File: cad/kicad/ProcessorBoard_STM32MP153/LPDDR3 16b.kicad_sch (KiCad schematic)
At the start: 6 parts, among them U401 XT61M2G8D2TA-B8BEA

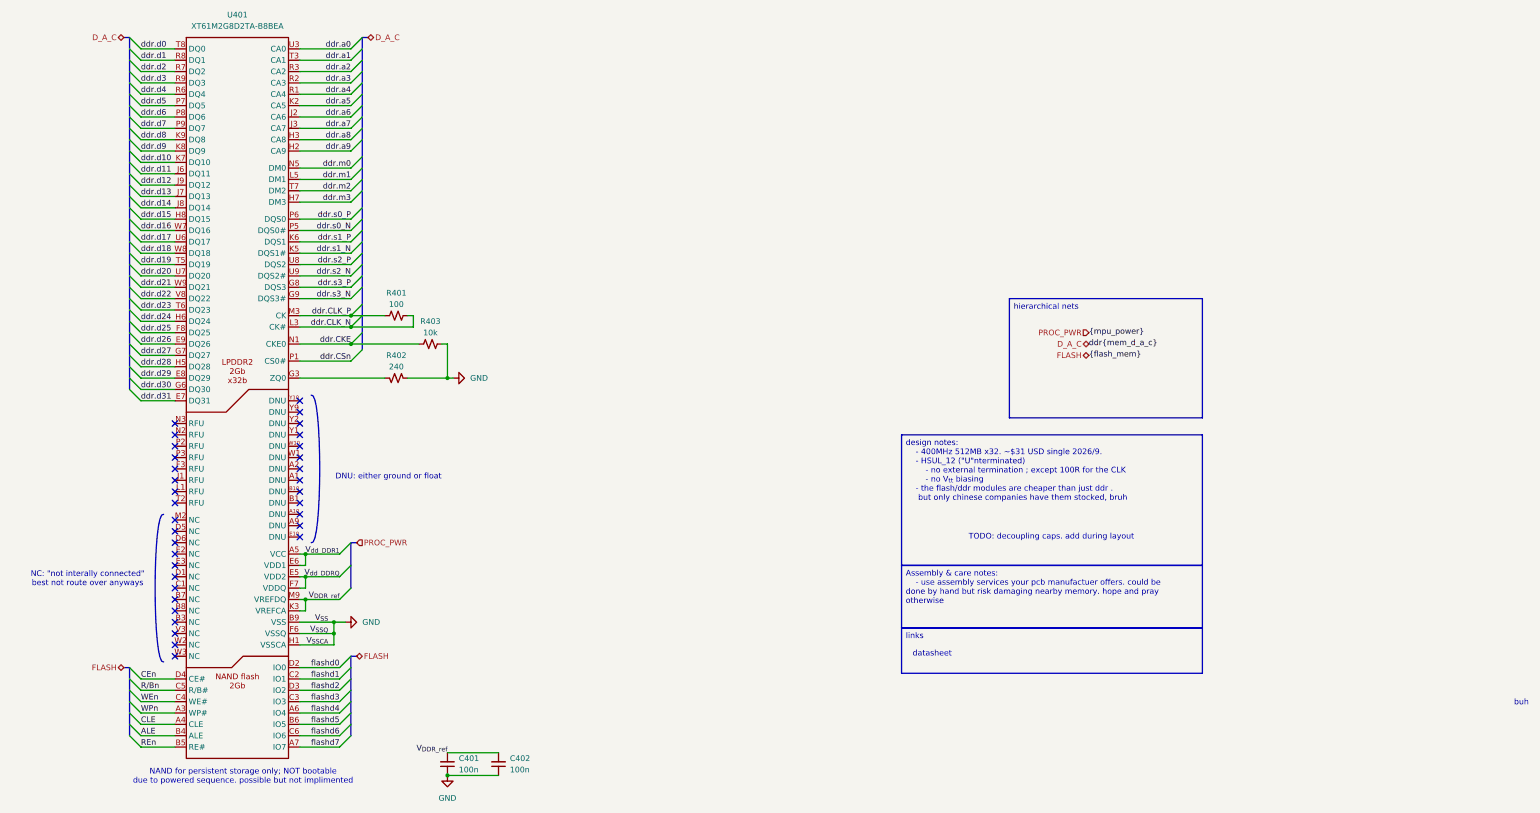
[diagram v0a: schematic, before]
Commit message: 2 layer ddr route. un tuned, missing pwr
initial ddr rout done, not lenght tuned, only impedance matched. layer 1 completely free of traces, need to put power planes on it
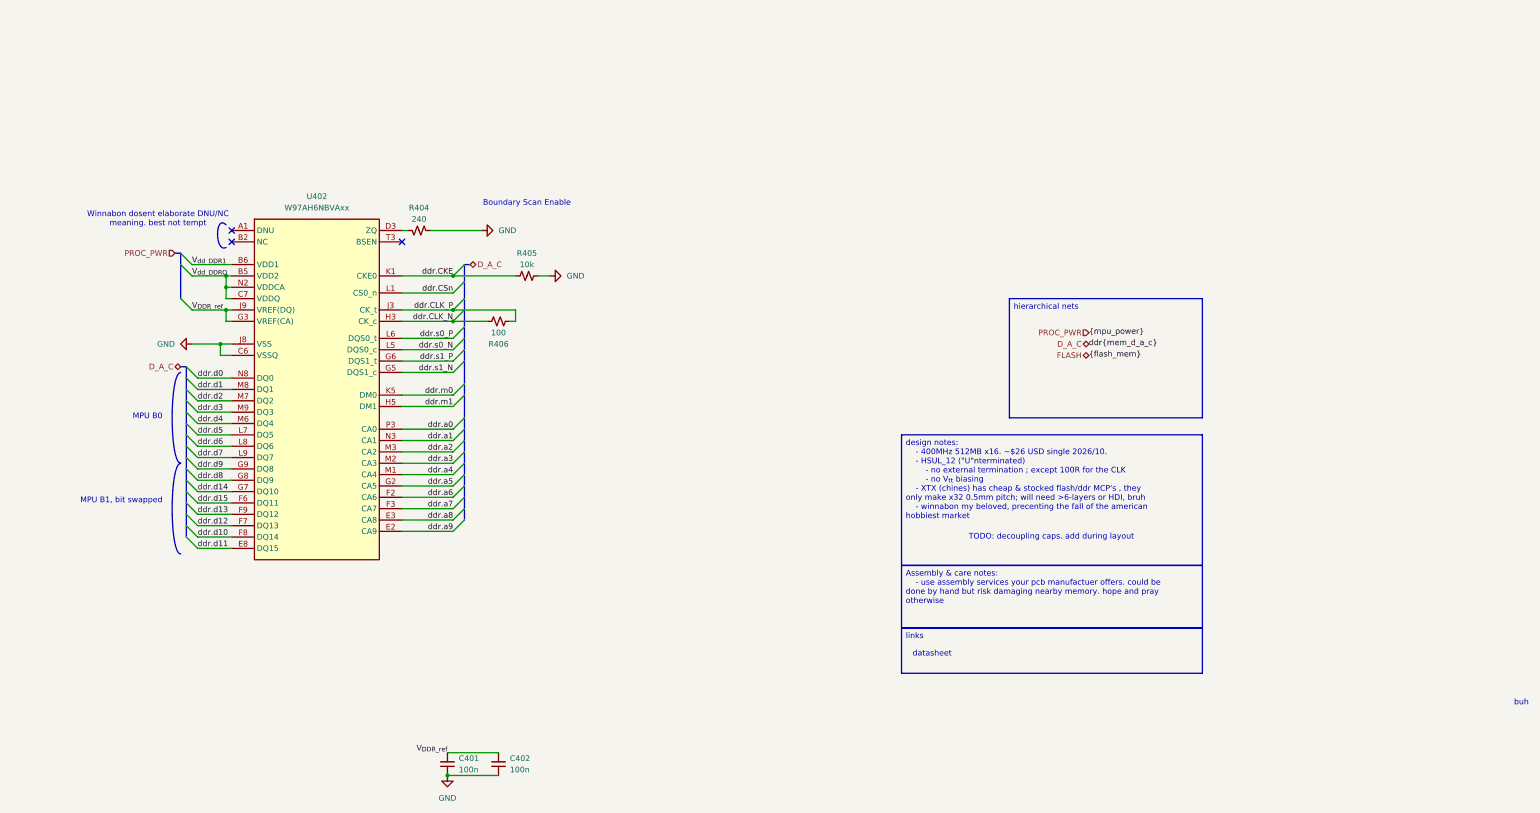
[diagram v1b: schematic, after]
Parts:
- removed R401: 100, Resistor_SMD:R_0402_1005Metric_Pad0.72x0.64mm_HandSolder, symbol Device:R_Small_US
- removed R402: 240, Capacitor_SMD:C_0402_1005Metric_Pad0.74x0.62mm_HandSolder, symbol Device:R_Small_US
- removed R403: 10k, Resistor_SMD:R_0603_1608Metric_Pad0.98x0.95mm_HandSolder, symbol Device:R_Small_US
- removed U401: XT61M2G8D2TA-B8BEA, __WM_Local:FBGA-162_L10.5-W8.0-P0.50_XT61M4G8D2TA, symbol __WM_Local:XT61M2G8D2TA-B8BEA
- added R404: 240, Capacitor_SMD:C_0402_1005Metric_Pad0.74x0.62mm_HandSolder, symbol Device:R_Small_US
- added R405: 10k, Resistor_SMD:R_0603_1608Metric_Pad0.98x0.95mm_HandSolder, symbol Device:R_Small_US
- added R406: 100, Resistor_SMD:R_0402_1005Metric_Pad0.72x0.64mm_HandSolder, symbol Device:R_Small_US
- added U402: W97AH6NBVAxx, __WM_Local:BGA134C65P10X17_1000X1150X110, symbol __WM_Local:W97AH6NBVAxx
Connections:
- net GND: now also R404.2, R405.2, U402.C2 (VSS), U402.C5 (VSS), U402.C6 (VSSQ), U402.C9 (VSSQ), U402.D1 (VSS), U402.D10 (VSSQ), U402.E1 (VSS), U402.E10 (VSSQ), U402.F5 (VSSQ), U402.G10 (VSSQ), U402.H2 (VSS), U402.J1 (VSS), U402.J5 (VSSQ), U402.J8 (VSS), U402.L10 (VSSQ), U402.M5 (VSSQ), U402.N1 (VSS), U402.N10 (VSSQ), U402.P1 (VSS), U402.P10 (VSSQ), U402.R2 (VSS), U402.R5 (VSS), U402.R6 (VSSQ), U402.R9 (VSSQ)
- net V_{DDR_ref}: now also U402.G3 (VREF(CA)), U402.J9 (VREF(DQ))
- net V_{dd_DDR1}: now also U402.B6 (VDD1), U402.C1 (VDD1), U402.R1 (VDD1), U402.T6 (VDD1)
- net V_{dd_DDRQ}: now also U402.B5 (VDD2), U402.C10 (VDDQ), U402.C7 (VDDQ), U402.D2 (VDD2), U402.D5 (VDDQ), U402.E9 (VDDQ), U402.F1 (VDDCA), U402.F10 (VDDQ), U402.G1 (VDD2), U402.H1 (VDDCA), U402.H6 (VDDQ), U402.J6 (VDDQ), U402.J7 (VDD2), U402.K6 (VDDQ), U402.M10 (VDDQ), U402.N2 (VDDCA), U402.N9 (VDDQ), U402.P2 (VDD2), U402.P5 (VDDQ), U402.R10 (VDDQ), U402.R7 (VDDQ), U402.T5 (VDD2)
- net ddr.CKE: now also R405.1, U402.K1 (CKE0)
- net ddr.CLK_N: now also R406.2, U402.H3 (CK_c)
- net ddr.CLK_P: now also R406.1, U402.J3 (CK_t)
- net ddr.CSn: now also U402.L1 (CS0_n)
- net ddr.a0: now also U402.P3 (CA0)
- net ddr.a1: now also U402.N3 (CA1)
- net ddr.a2: now also U402.M3 (CA2)
- net ddr.a3: now also U402.M2 (CA3)
- net ddr.a4: now also U402.M1 (CA4)
- net ddr.a5: now also U402.G2 (CA5)
- net ddr.a6: now also U402.F2 (CA6)
- net ddr.a7: now also U402.F3 (CA7)
- net ddr.a8: now also U402.E3 (CA8)
- net ddr.a9: now also U402.E2 (CA9)
- net ddr.d0: now also U402.N8 (DQ0)
- net ddr.d1: now also U402.M8 (DQ1)
- net ddr.d10: now also U402.F8 (DQ14)
- net ddr.d11: now also U402.E8 (DQ15)
- net ddr.d12: now also U402.F7 (DQ13)
- net ddr.d13: now also U402.F9 (DQ12)
- net ddr.d14: now also U402.G7 (DQ10)
- net ddr.d15: now also U402.F6 (DQ11)
- net ddr.d2: now also U402.M7 (DQ2)
- net ddr.d3: now also U402.M9 (DQ3)
- net ddr.d4: now also U402.M6 (DQ4)
- net ddr.d5: now also U402.L7 (DQ5)
- net ddr.d6: now also U402.L8 (DQ6)
- net ddr.d7: now also U402.L9 (DQ7)
- net ddr.d8: now also U402.G8 (DQ9)
- net ddr.d9: now also U402.G9 (DQ8)
- net ddr.m0: now also U402.K5 (DM0)
- net ddr.m1: now also U402.H5 (DM1)
- net ddr.s0_N: now also U402.L5 (DQS0_c)
- net ddr.s0_P: now also U402.L6 (DQS0_t)
- net ddr.s1_N: now also U402.G5 (DQS1_c)
- net ddr.s1_P: now also U402.G6 (DQS1_t)
- new net: U402.A1 (DNU), U402.A10 (DNU), U402.A2 (DNU), U402.A9 (DNU), U402.B1 (DNU), U402.B10 (DNU), U402.T1 (DNU), U402.T10 (DNU), U402.U1 (DNU), U402.U10 (DNU), U402.U2 (DNU), U402.U9 (DNU)
- new net: U402.B2 (NC), U402.B3 (NC), U402.B7 (NC), U402.B8 (NC), U402.B9 (NC), U402.C3 (NC), U402.C8 (NC), U402.D6 (NC), U402.D7 (NC), U402.D8 (NC), U402.D9 (NC), U402.E5 (NC), U402.E6 (NC), U402.E7 (NC), U402.J2 (NC), U402.K2 (NC), U402.K3 (NC), U402.L2 (NC), U402.L3 (NC), U402.N5 (NC), U402.N6 (NC), U402.N7 (NC), U402.P6 (NC), U402.P7 (NC), U402.P8 (NC), U402.P9 (NC), U402.R3 (NC), U402.R8 (NC), U402.T2 (NC), U402.T7 (NC), U402.T8 (NC), U402.T9 (NC)
- new net: R404.1, U402.D3 (ZQ)
- no-connect marks 34 -> 3
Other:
- note added: "Boundary Scan Enable"
- note added: "MPU B0"
- note added: "MPU B1, bit swapped"
- note added: "Winnabon dosent elaborate DNU/NC meaning. best not tempt"
- note removed: "DNU: either ground or float"
- note removed: "NAND for persistent storage only; NOT bootable due to powered sequence. possible but not implimented"
- note removed: "NC: "not interally connected" best not route over anyways"

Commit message: good enuff routing
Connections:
- net ddr.d11: now also U402.F7 (DQ13); no longer U402.E8 (DQ15)
- net ddr.d12: now also U402.E8 (DQ15); no longer U402.F7 (DQ13)
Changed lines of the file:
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@@
 	)
 	(label "ddr.d11"
-		(at 58.42 137.16 0)
+		(at 58.42 132.08 0)
 		(effects
 			(font
@@
 	)
 	(label "ddr.d12"
-		(at 58.42 132.08 0)
+		(at 58.42 137.16 0)
 		(effects
 			(font

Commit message: boo womp 10000
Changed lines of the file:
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@@
 	(text "Boundary Scan Enable\n"
 		(exclude_from_sim no)
-		(at 132.08 59.944 0)
+		(at 105.918 68.834 0)
 		(effects
 			(font
 				(size 1.27 1.27)
 			)
+			(justify left)
 		)
 	)

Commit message: i forgor track spacing :(
need to redo ddr
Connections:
- net ddr.d10: now also U402.G7 (DQ10); no longer U402.F8 (DQ14)
- net ddr.d12: now also U402.F9 (DQ12); no longer U402.E8 (DQ15)
- net ddr.d13: now also U402.E8 (DQ15); no longer U402.F9 (DQ12)
- net ddr.d14: now also U402.F8 (DQ14); no longer U402.G7 (DQ10)
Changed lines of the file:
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@@
 	)
 	(label "ddr.d13"
-		(at 58.42 129.54 0)
+		(at 58.42 137.16 0)
 		(effects
 			(font
@@
 	)
 	(label "ddr.d12"
-		(at 58.42 137.16 0)
+		(at 58.42 129.54 0)
 		(effects
 			(font
@@
 	)
 	(label "ddr.d14"
-		(at 58.42 124.46 0)
+		(at 58.42 134.62 0)
 		(effects
 			(font
@@
 	)
 	(label "ddr.d10"
-		(at 58.42 134.62 0)
+		(at 58.42 124.46 0)
 		(effects
 			(font

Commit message: ddr shuffle maxxing round 2
mostly hitting the 3w and 4w spacing. one must hope. #hope
ive disabled DRC for optimal routing experience . ching chong over clank ckong any day(until i get the good stuff) has nothing on the sweat shop.
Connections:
- net ddr.d10: now also U402.E8 (DQ15); no longer U402.G7 (DQ10)
- net ddr.d11: now also U402.F8 (DQ14); no longer U402.F7 (DQ13)
- net ddr.d12: now also U402.F6 (DQ11); no longer U402.F9 (DQ12)
- net ddr.d13: now also U402.F7 (DQ13); no longer U402.E8 (DQ15)
- net ddr.d14: now also U402.F9 (DQ12); no longer U402.F8 (DQ14)
- net ddr.d15: now also U402.G8 (DQ9); no longer U402.F6 (DQ11)
- net ddr.d8: now also U402.G7 (DQ10); no longer U402.G8 (DQ9)
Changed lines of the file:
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@@
 	)
 	(label "ddr.d8"
-		(at 58.42 121.92 0)
+		(at 58.42 124.46 0)
 		(effects
 			(font
@@
 	)
 	(label "ddr.d13"
-		(at 58.42 137.16 0)
+		(at 58.42 132.08 0)
 		(effects
 			(font
@@
 	)
 	(label "ddr.d11"
-		(at 58.42 132.08 0)
+		(at 58.42 134.62 0)
 		(effects
 			(font
@@
 	)
 	(label "ddr.d12"
-		(at 58.42 129.54 0)
+		(at 58.42 127 0)
 		(effects
 			(font
@@
 	)
 	(label "ddr.d14"
-		(at 58.42 134.62 0)
+		(at 58.42 129.54 0)
 		(effects
 			(font
@@
 	)
 	(label "ddr.d15"
-		(at 58.42 127 0)
+		(at 58.42 121.92 0)
 		(effects
 			(font
@@
 	)
 	(label "ddr.d10"
-		(at 58.42 124.46 0)
-		(effects
-			(font
+		(at 58.42 137.16 0)
+		(effects
+			(font

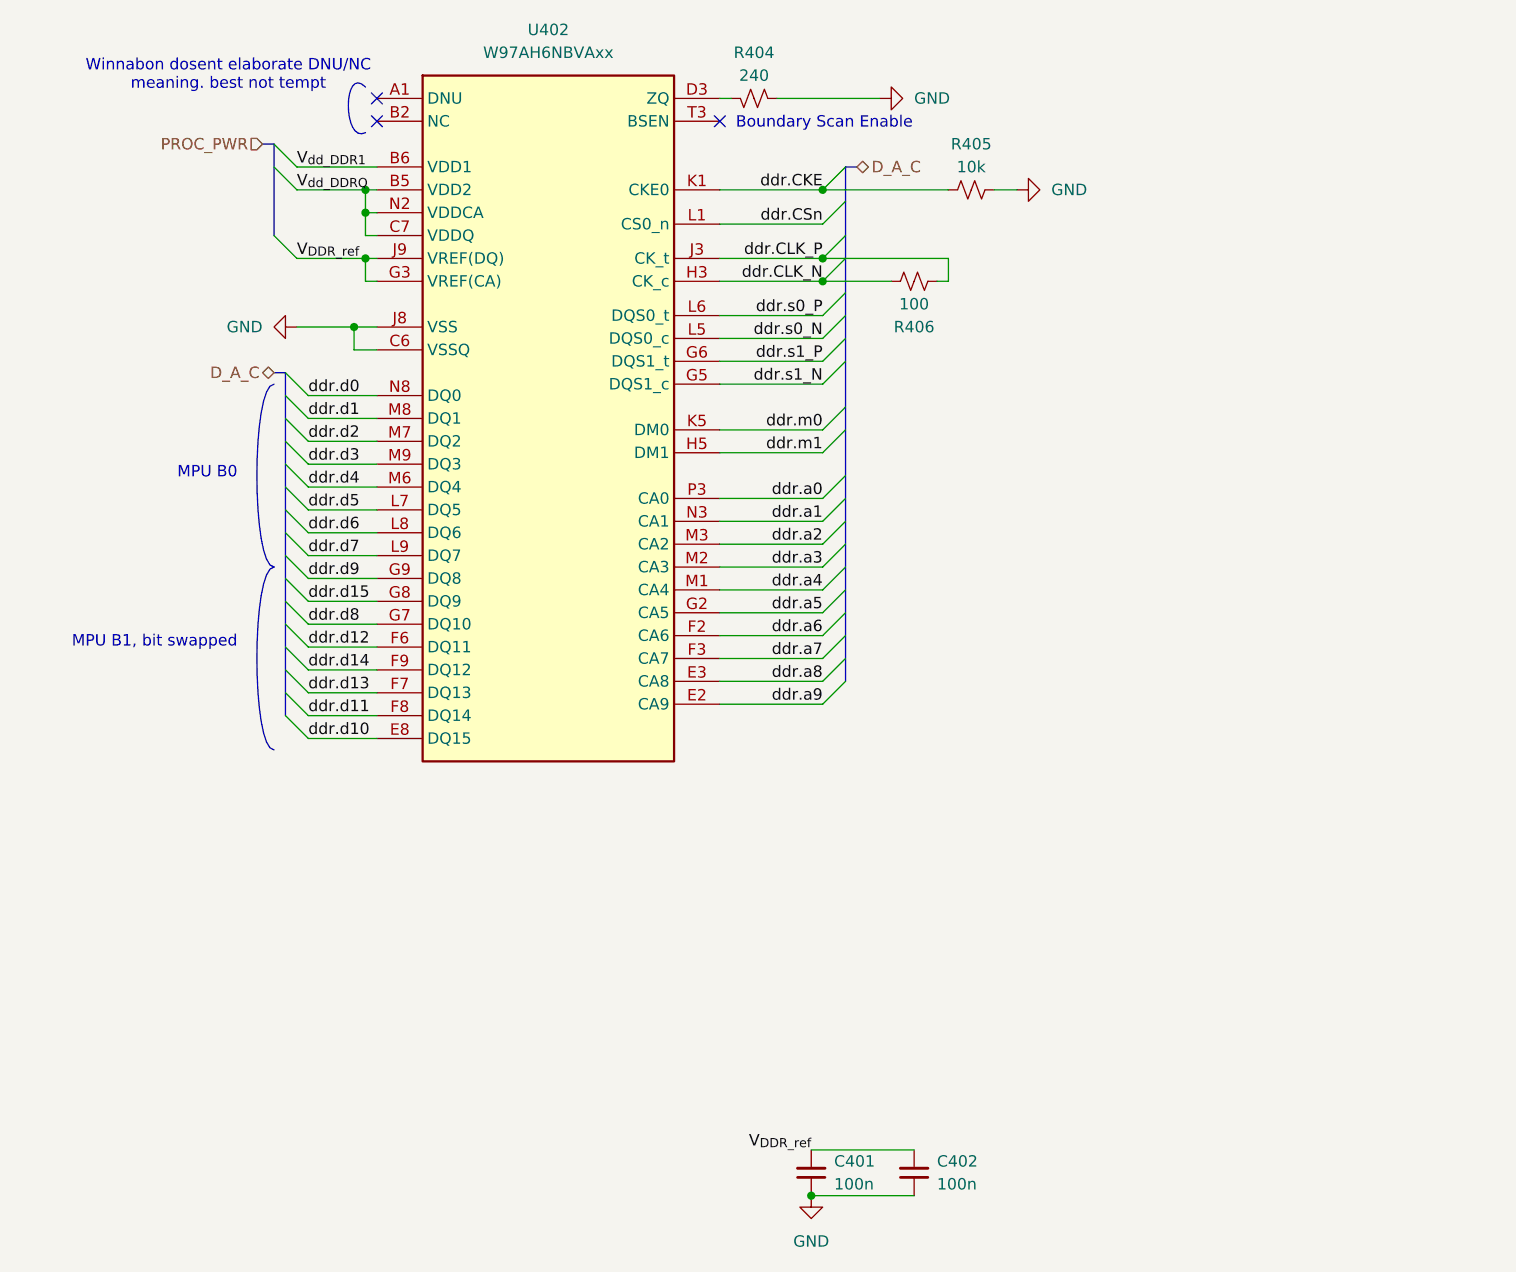
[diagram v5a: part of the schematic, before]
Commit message: shuffled core back to left side of board, fits better
row row the power planes under mpu
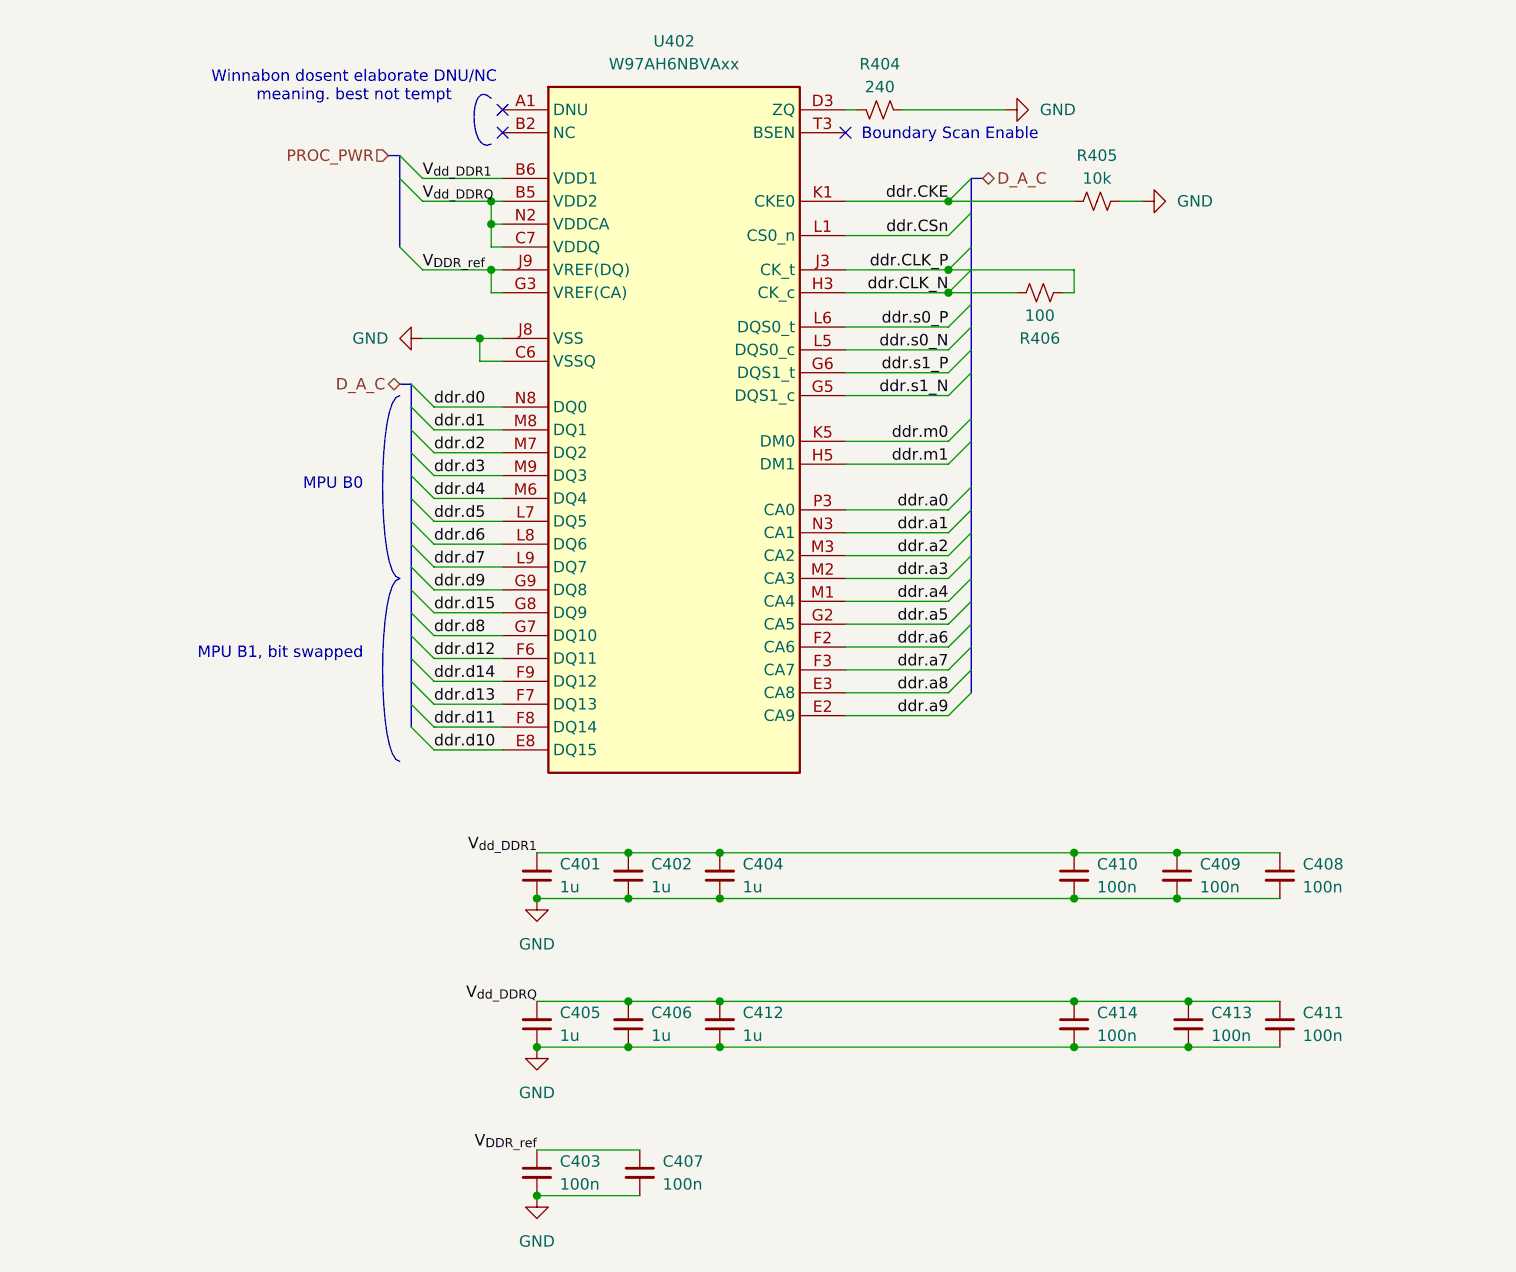
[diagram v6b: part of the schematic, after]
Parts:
- added C403, C407, C408, C409, C410, C411, C413, C414: 100n, Capacitor_SMD:C_0402_1005Metric, symbol Device:C_Small
- added C404, C405, C406, C412: 1u, Capacitor_SMD:C_0402_1005Metric, symbol Device:C_Small
- C401, C402: value 100n -> 1u; footprint Capacitor_SMD:C_0402_1005Metric_Pad0.74x0.62mm_HandSolder -> Capacitor_SMD:C_0402_1005Metric; character http://ksim.kemet.com/?pn=C0402C104K4PAC7411&disty=mouser -> https://ds.murata.com/simsurfing/mlcc.html?partnumbers=%5B%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; mouser https://www.mouser.com/en/ProductDetail/KEMET/C0402C104K4PA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 -> https://www.mouser.com/en/ProductDetail/Murata-Electronics/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; unit x1 0.10 -> 0.11; unit x10 0.048 -> 0.04
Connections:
- net GND: now also C403.2, C404.1, C405.1, C406.1, C407.2, C408.2, C409.2, C410.2, C411.2, C412.1, C413.2, C414.2
- net V_{DDR_ref}: now also C403.1, C407.1; no longer C401.2, C402.2
- net V_{dd_DDR1}: now also C401.2, C402.2, C404.2, C408.1, C409.1, C410.1
- net V_{dd_DDRQ}: now also C405.2, C406.2, C411.1, C412.2, C413.1, C414.1
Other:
- moved on the sheet: R404, R405, R406, U402
